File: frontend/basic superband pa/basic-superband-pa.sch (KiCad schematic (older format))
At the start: 59 parts, among them CN1 EDGE, CN2 BREAKOUT, K1 D3002, K2 D3002, P1 BNC, P2 CONN_02X01, P3 CONN_01X02, Q1 NPN, Q2 PNP, Q3 RD16HHF1, T1 TRANSFO, T2 8:1, T3 4:1, T4 OUT_TRANSF, U1 LP2951-50D

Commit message: Board files updated
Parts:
- added Q4: NPN, Transistors_SMD:sot23, symbol NPN
- added R10, R12: DNI, HERMESLITE:R_0805, symbol R
- added R11: 0, HERMESLITE:R_0805, symbol R
- added R9: 4.99k, HERMESLITE:R_0805, symbol R
- C22: value 47uF 16V -> 10uF 16V; footprint Discret:C1V8 -> Capacitors_Tantalum_SMD:TantalC_SizeB_EIA-3528_Reflow
- Q3: footprint Transistors_TO-220:TO-220_Neutral123_Horizontal -> Transistors_TO-220:TO-220_Neutral123_Vertical
- R8: value 2.21k -> 10k
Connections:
- wire segments 169 -> 181
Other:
- note added: "(Assuming CMOS inputs so\nbuffering to reduce loading.\nPTT# - RX=high, TX=low\nGPIO0 = BS0=low, BS1=high)"
- note added: "BAND 1"
- note added: "Band 0"
- note removed: "(RX=high, TX=low)"

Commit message: Upload latest pcb changes
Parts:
- removed CN2: BREAKOUT, Pin_Headers:Pin_Header_Straight_1x12, symbol BREAKOUT
- removed P3: CONN_01X02, Pin_Headers:Pin_Header_Straight_1x02, symbol CONN_01X02
- removed Q4: NPN, Transistors_SMD:sot23, symbol NPN
- removed R9: 4.99k, HERMESLITE:R_0805, symbol R
- added C25, C26, C27, C28: 0.01uF, HERMESLITE:C_0805, symbol C
- added C29: 0.1uF, HERMESLITE:C_0805, symbol C
- L10: footprint Choke_Axial_ThroughHole:Choke_Horizontal_RM10mm -> Choke_Toroid_ThroughHole:Choke_Toroid_horizontal_Diameter3-5mm_Amidon-T12
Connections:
- wire segments 181 -> 155
- no-connect marks 4 -> 17
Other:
- note added: "PTT# - RX=high, TX=low\nGPIO0 = BS0=low, BS1=high"
- note removed: "(Assuming CMOS inputs so\nbuffering to reduce loading.\nPTT# - RX=high, TX=low\nGPIO0 = BS0=low, BS1=high)"
- note removed: "Note: For superband PAs\nAlex protocol is disabled and \nGPIO0 is band select.\n\nCN2 will be removed after circuit prototype phase complete.\n\n"
- moved on the sheet: R1

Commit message: BOM updates
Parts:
- renumbered C8 to C11, C9 to C13, C11 to C14, C13 to C4, C4 to C5, C14 to C7, C5 to C8, C7 to C9, L3 to L2, L4 to L3, L2 to L4, L8 to L5, L5 to L7, L7 to L8
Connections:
- net at C11.1, K1.4 (T1), L7.1: now also C14.1
- net at K1.7 (T2), L5.2: no longer C14.1
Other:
- moved on the sheet: C14
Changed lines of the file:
@@
 GPIO0
 $Comp
-L INDUCTOR L5
+L INDUCTOR L7
 U 1 1 547D41C7
 P 3700 7450
-F 0 "L5" V 3650 7450 40  0000 C CNN
+F 0 "L7" V 3650 7450 40  0000 C CNN
 F 1 "INDUCTOR" V 3800 7450 40  0001 C CNN
 F 2 "Choke_Toroid_ThroughHole:Choke_Toroid_6,5x13mm_Vertical" H 3700 7450 60  0001 C CNN
@@
 $EndComp
 $Comp
-L C C8
+L C C11
 U 1 1 547D43ED
 P 3900 7150
-F 0 "C8" V 3850 6950 40  0000 L CNN
+F 0 "C11" V 3850 6950 40  0000 L CNN
 F 1 "C" H 3906 7065 40  0001 L CNN
 F 2 "HERMESLITE:C_0805" H 3938 7000 30  0001 C CNN
@@
 $EndComp
 $Comp
-L C C9
+L C C13
 U 1 1 547D44ED
 P 4700 7350
-F 0 "C9" H 4700 7450 40  0000 L CNN
+F 0 "C13" H 4700 7450 40  0000 L CNN
 F 1 "C" H 4706 7265 40  0001 L CNN
 F 2 "HERMESLITE:C_0805" H 4738 7200 30  0001 C CNN
@@
 $EndComp
 $Comp
-L INDUCTOR L7
+L INDUCTOR L8
 U 1 1 547D4686
 P 4850 7450
-F 0 "L7" V 4800 7450 40  0000 C CNN
+F 0 "L8" V 4800 7450 40  0000 C CNN
 F 1 "INDUCTOR" V 4950 7450 40  0001 C CNN
 F 2 "Choke_Toroid_ThroughHole:Choke_Toroid_6,5x13mm_Vertical" H 4850 7450 60  0001 C CNN
@@
 $EndComp
 $Comp
-L INDUCTOR L8
+L INDUCTOR L5
 U 1 1 547D490A
 P 5550 7150
-F 0 "L8" V 5500 7150 40  0000 C CNN
+F 0 "L5" V 5500 7150 40  0000 C CNN
 F 1 "INDUCTOR" V 5650 7150 40  0001 C CNN
 F 2 "Choke_Toroid_ThroughHole:Choke_Toroid_6,5x13mm_Vertical" H 5550 7150 60  0001 C CNN
@@
 $EndComp
 $Comp
-L C C11
+L C C14
 U 1 1 547D4975
-P 5850 7350
-F 0 "C11" H 5850 7450 40  0000 L CNN
-F 1 "C" H 5856 7265 40  0001 L CNN
-F 2 "HERMESLITE:C_0805" H 5888 7200 30  0001 C CNN
-F 3 "" H 5850 7350 60  0000 C CNN
-	1    5850 7350
-	1    0    0    -1
-$EndComp
-$Comp
-L INDUCTOR L4
+P 3450 7350
+F 0 "C14" H 3450 7450 40  0000 L CNN
+F 1 "C" H 3456 7265 40  0001 L CNN
+F 2 "HERMESLITE:C_0805" H 3488 7200 30  0001 C CNN
+F 3 "" H 3450 7350 60  0000 C CNN
+	1    3450 7350
+	1    0    0    -1
+$EndComp
+$Comp
+L INDUCTOR L3
 U 1 1 547D4CF1
 P 6000 6500
-F 0 "L4" V 5950 6500 40  0000 C CNN
+F 0 "L3" V 5950 6500 40  0000 C CNN
 F 1 "INDUCTOR" V 6100 6500 40  0001 C CNN
 F 2 "Choke_Toroid_ThroughHole:Choke_Toroid_6,5x13mm_Vertical" H 6000 6500 60  0001 C CNN
@@
 $EndComp
 $Comp
-L C C4
+L C C5
 U 1 1 547D4CF8
 P 4500 6200
-F 0 "C4" V 4450 6300 40  0000 L CNN
+F 0 "C5" V 4450 6300 40  0000 L CNN
 F 1 "C" H 4506 6115 40  0001 L CNN
 F 2 "HERMESLITE:C_0805" H 4538 6050 30  0001 C CNN
@@
 $EndComp
 $Comp
-L C C5
+L C C8
 U 1 1 547D4D04
 P 4700 6400
-F 0 "C5" H 4700 6500 40  0000 L CNN
+F 0 "C8" H 4700 6500 40  0000 L CNN
 F 1 "C" H 4706 6315 40  0001 L CNN
 F 2 "HERMESLITE:C_0805" H 4738 6250 30  0001 C CNN
@@
 $EndComp
 $Comp
-L INDUCTOR L2
+L INDUCTOR L4
 U 1 1 547D4D0B
 P 4850 6500
-F 0 "L2" V 4800 6500 40  0000 C CNN
+F 0 "L4" V 4800 6500 40  0000 C CNN
 F 1 "INDUCTOR" V 4950 6500 40  0001 C CNN
 F 2 "Choke_Toroid_ThroughHole:Choke_Toroid_6,5x13mm_Vertical" H 4850 6500 60  0001 C CNN
@@
 $EndComp
 $Comp
-L INDUCTOR L3
+L INDUCTOR L2
 U 1 1 547D4D17
 P 5150 6200
-F 0 "L3" V 5100 6200 40  0000 C CNN
+F 0 "L2" V 5100 6200 40  0000 C CNN
 F 1 "INDUCTOR" V 5250 6200 40  0001 C CNN
 F 2 "Choke_Toroid_ThroughHole:Choke_Toroid_6,5x13mm_Vertical" H 5150 6200 60  0001 C CNN
@@
 $EndComp
 $Comp
-L C C7
+L C C9
 U 1 1 547D4D1D
 P 5850 6400
-F 0 "C7" H 5850 6500 40  0000 L CNN
+F 0 "C9" H 5850 6500 40  0000 L CNN
 F 1 "C" H 5856 6315 40  0001 L CNN
 F 2 "HERMESLITE:C_0805" H 5888 6250 30  0001 C CNN
@@
 L GND #PWR012
 U 1 1 547D5D63
-P 5850 7550
-F 0 "#PWR012" H 5850 7550 30  0001 C CNN
-F 1 "GND" H 5850 7480 30  0001 C CNN
-F 2 "" H 5850 7550 60  0000 C CNN
-F 3 "" H 5850 7550 60  0000 C CNN
-	1    5850 7550
+P 3450 7550
+F 0 "#PWR012" H 3450 7550 30  0001 C CNN
+F 1 "GND" H 3450 7480 30  0001 C CNN
+F 2 "" H 3450 7550 60  0000 C CNN
+F 3 "" H 3450 7550 60  0000 C CNN
+	1    3450 7550
 	1    0    0    -1
 $EndComp
@@
 $EndComp
 $Comp
-L CP1 C14
+L CP1 C7
 U 1 1 54872CD7
 P 5250 1750
-F 0 "C14" H 5300 1850 50  0000 L CNN
+F 0 "C7" H 5300 1850 50  0000 L CNN
 F 1 "47uF 16V" H 5400 1750 50  0000 L CNN
 F 2 "Discret:C1V8" H 5250 1750 60  0001 C CNN
@@
 $EndComp
 $Comp
-L C C13
+L C C4
 U 1 1 54872F5F
 P 5000 1750
-F 0 "C13" H 5000 1850 40  0000 L CNN
+F 0 "C4" H 5000 1850 40  0000 L CNN
 F 1 "0.1uF" H 4800 1850 40  0000 L CNN
 F 2 "HERMESLITE:C_0805" H 5038 1600 30  0001 C CNN
@@
 	1    0    0    -1
 $EndComp
-Text Notes 2550 7600 0    40   ~ 0
+Text Notes 2450 7550 0    40   ~ 0
 (Omit K2 and wire directly \nif only 1 band pair desired)
 $Comp
@@
 Connection ~ 4850 7750
 Connection ~ 4700 7550
-Connection ~ 5850 7550
+Connection ~ 3450 7550
 Connection ~ 3700 7750
 Connection ~ 4700 6600
@@
 Wire Wire Line
 	10200 5400 10200 6000
+Connection ~ 3450 7150
 $EndSCHEMATC

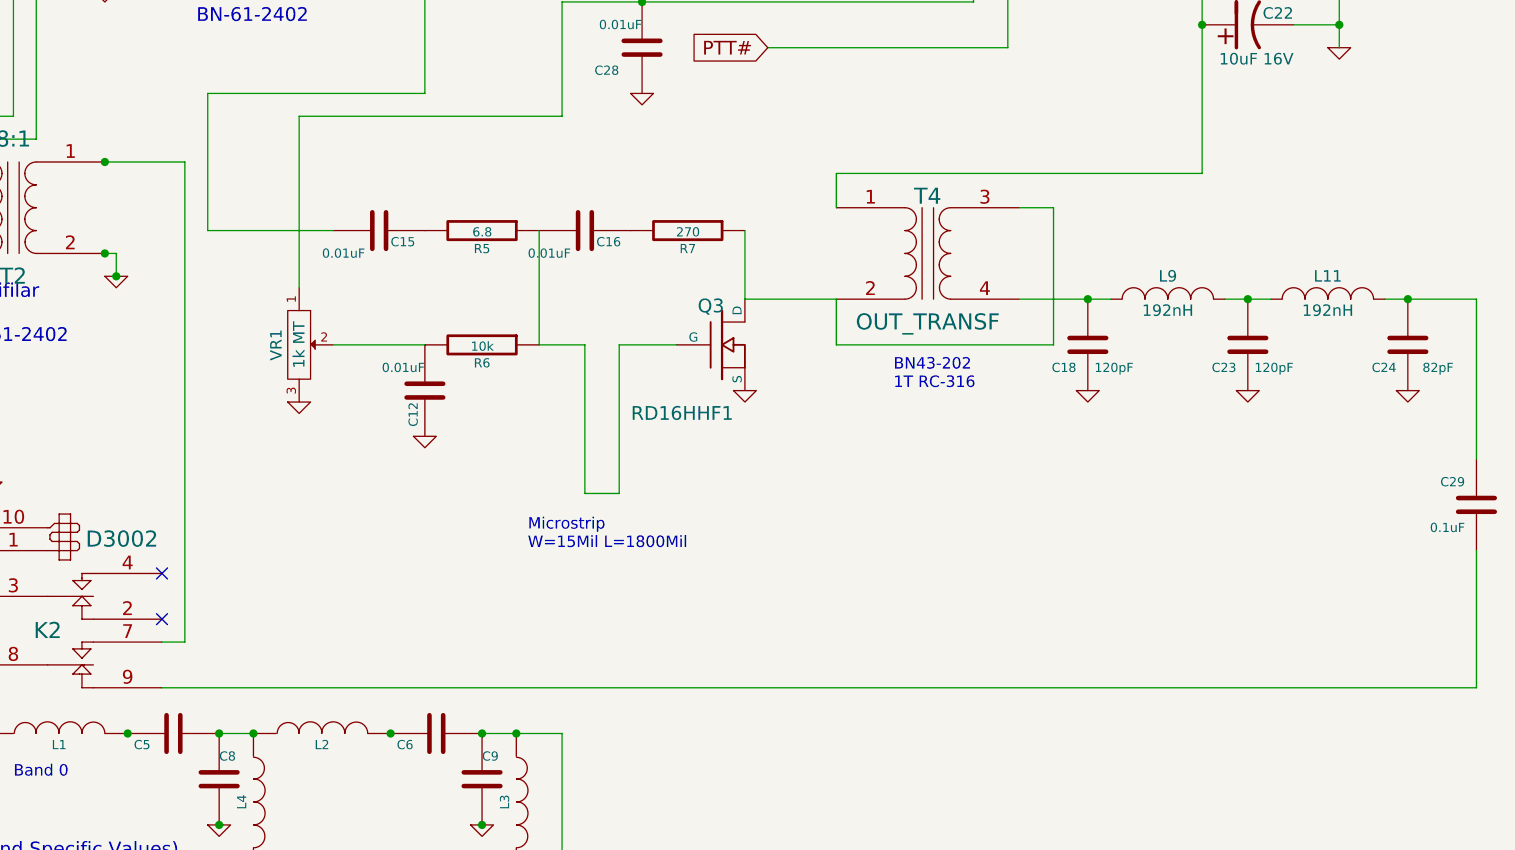
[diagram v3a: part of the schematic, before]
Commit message: Correct compnent naming and fix relay error
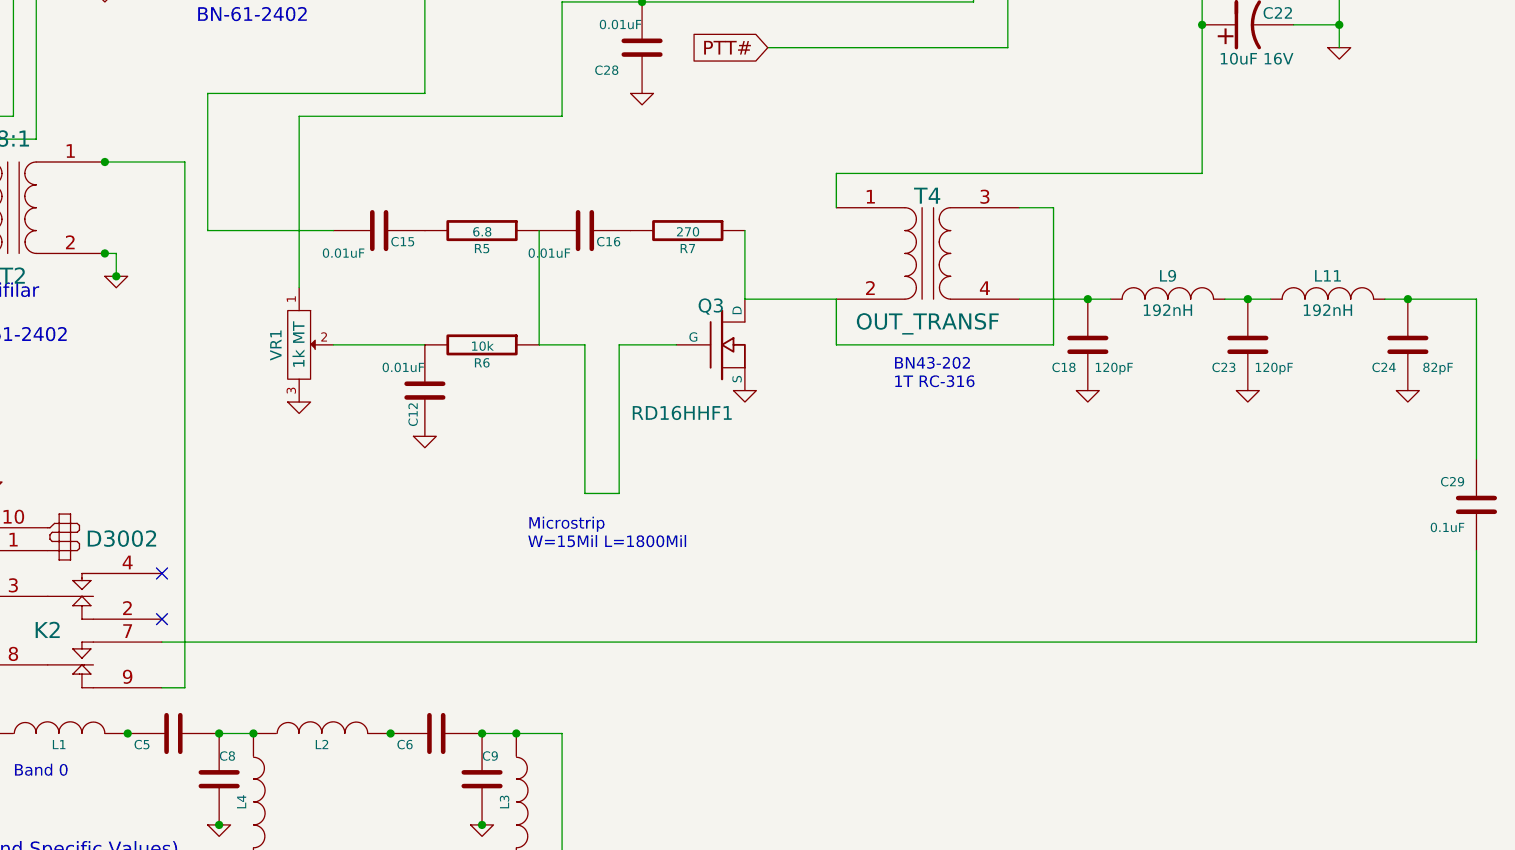
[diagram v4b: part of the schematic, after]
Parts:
- C22: footprint Capacitors_Tantalum_SMD:TantalC_SizeB_EIA-3528_Reflow -> Capacitors_SMD:C_1206
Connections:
- net at T2.1 (S1): now also K2.9 (R2); no longer K2.7 (T2)
- net at C29.1: now also K2.7 (T2); no longer K2.9 (R2)
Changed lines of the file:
@@
 F 0 "C22" V 9250 2900 50  0000 L CNN
 F 1 "10uF 16V" V 9050 2900 50  0000 L CNN
-F 2 "Capacitors_Tantalum_SMD:TantalC_SizeB_EIA-3528_Reflow" H 9200 3100 60  0001 C CNN
+F 2 "Capacitors_SMD:C_1206" H 9200 3100 60  0001 C CNN
 F 3 "" H 9200 3100 60  0000 C CNN
 	1    9200 3100
@@
 	1    2700 5650
 	1    0    0    -1
-$EndComp
-$Comp
-L D3002 K2
-U 1 1 54AF7B3F
-P 4050 5650
-F 0 "K2" H 3950 5750 70  0000 C CNN
-F 1 "D3002" H 4275 5350 70  0000 C CNN
-F 2 "HERMESLITE:D3002" H 4050 5650 60  0001 C CNN
-F 3 "" H 4050 5650 60  0000 C CNN
-	1    4050 5650
-	1    0    0    1
 $EndComp
 $Comp
@@
 	2400 7050 2500 7050
 Wire Wire Line
-	4550 3700 4550 5800
+	4550 3700 4550 6000
 Wire Wire Line
 	3400 4650 3400 4600
@@
 	3200 5900 3650 5900
 Wire Wire Line
-	4550 5800 4450 5800
-Wire Wire Line
 	3700 5100 3700 5000
 Wire Wire Line
@@
 Wire Wire Line
 	3600 5300 3650 5300
-Wire Wire Line
-	10200 6000 4450 6000
 Wire Wire Line
 	6450 5150 6300 5150
@@
 Wire Wire Line
 	10200 4300 10200 5000
-Wire Wire Line
-	10200 5400 10200 6000
 Connection ~ 3450 7150
+$Comp
+L D3002 K2
+U 1 1 54AF7B3F
+P 4050 5650
+F 0 "K2" H 3950 5750 70  0000 C CNN
+F 1 "D3002" H 4275 5350 70  0000 C CNN
+F 2 "HERMESLITE:D3002" H 4050 5650 60  0001 C CNN
+F 3 "" H 4050 5650 60  0000 C CNN
+	1    4050 5650
+	1    0    0    1
+$EndComp
+Wire Wire Line
+	4550 6000 4450 6000
+Wire Wire Line
+	4450 5800 10200 5800
+Wire Wire Line
+	10200 5800 10200 5400
 $EndSCHEMATC

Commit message: Few more pcb changes
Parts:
- added JP1: JUMPER4, HERMESLITE:JUMPER4, symbol JUMPER4
- added R13: 4.99k, HERMESLITE:R_0805, symbol R
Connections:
- net GND: now also JP1.1
- net GPIO0: now also JP1.4; no longer R1.2
- net at C17.1, C26.2, C4.1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: now also R13.1
- new net: JP1.2, R1.2
- new net: JP1.3, R13.2
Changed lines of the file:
@@
 	1    0    0    -1
 $EndComp
-Text GLabel 1800 5650 0    60   Input ~ 0
+Text GLabel 1150 5650 0    60   Input ~ 0
 GPIO0
 Text GLabel 3900 1350 2    60   Output ~ 0
@@
 Text Notes 1400 7350 0    50   ~ 0
 BN-61-2402\n  2x4T #30
-Text Notes 1050 5350 0    60   ~ 0
+Text Notes 1500 4550 0    60   ~ 0
 PTT# - RX=high, TX=low\nGPIO0 = BS0=low, BS1=high
 Text Notes 3600 6750 0    60   ~ 0
@@
 Connection ~ 6550 3000
 Wire Wire Line
-	1800 5650 1900 5650
-Wire Wire Line
 	2400 5650 2500 5650
 Wire Wire Line
@@
 Connection ~ 2400 5650
 Connection ~ 2500 5650
-Connection ~ 1900 5650
 $Comp
 L C C26
@@
 Wire Wire Line
 	10200 5800 10200 5400
+$Comp
+L JUMPER4 JP1
+U 1 1 54BD04F7
+P 1650 5650
+F 0 "JP1" V 1750 5750 40  0000 L CNN
+F 1 "JUMPER4" V 1500 5450 40  0000 C CNN
+F 2 "HERMESLITE:JUMPER4" H 1650 5650 60  0001 C CNN
+F 3 "" H 1650 5650 60  0000 C CNN
+	1    1650 5650
+	0    -1   -1   0
+$EndComp
+$Comp
+L GND #PWR035
+U 1 1 54BD0629
+P 1650 5900
+F 0 "#PWR035" H 1650 5900 30  0001 C CNN
+F 1 "GND" H 1650 5830 30  0001 C CNN
+F 2 "" H 1650 5900 60  0000 C CNN
+F 3 "" H 1650 5900 60  0000 C CNN
+	1    1650 5900
+	1    0    0    -1
+$EndComp
+Wire Wire Line
+	1750 5650 1900 5650
+Wire Wire Line
+	1150 5650 1400 5650
+$Comp
+L R R13
+U 1 1 54BD0931
+P 1900 5400
+F 0 "R13" V 1980 5400 40  0000 C CNN
+F 1 "4.99k" V 1907 5401 40  0000 C CNN
+F 2 "HERMESLITE:R_0805" V 1830 5400 30  0001 C CNN
+F 3 "" H 1900 5400 30  0000 C CNN
+	1    1900 5400
+	0    1    1    0
+$EndComp
+Wire Wire Line
+	1300 5250 2200 5250
+Wire Wire Line
+	2200 5250 2200 5400
+Wire Wire Line
+	2200 5400 2150 5400
+Connection ~ 1300 5250
 $EndSCHEMATC

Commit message: Final pcd changes
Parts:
- added Q2-next: FDV301, symbol MOS_N
- R8: value 10k -> DNI
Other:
- note added: "DNI?"
- note added: "Need to pull up gate\nwith 10K to 3.3V"
- note added: "Remove in\nnext revision"
- note added: "Remove on next revision"
- note added: "Replace with 0R0"
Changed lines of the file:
@@
 	1    0    0    -1
 $EndComp
-Text Notes 3550 4500 0    60   ~ 0
+Text Notes 4000 3600 0    60   ~ 0
 6T bifilar\n4T\nBN-61-2402
 Text Notes 4600 3100 0    60   ~ 0
@@
 Text Notes 1400 7350 0    50   ~ 0
 BN-61-2402\n  2x4T #30
-Text Notes 1500 4550 0    60   ~ 0
+Text Notes 1700 4400 0    60   ~ 0
 PTT# - RX=high, TX=low\nGPIO0 = BS0=low, BS1=high
 Text Notes 3600 6750 0    60   ~ 0
@@
 P 8150 1800
 F 0 "R8" V 8230 1800 40  0000 C CNN
-F 1 "10k" V 8157 1801 40  0000 C CNN
+F 1 "DNI" V 8157 1801 40  0000 C CNN
 F 2 "HERMESLITE:R_0805" V 8080 1800 30  0001 C CNN
 F 3 "" H 8150 1800 30  0000 C CNN
@@
 	2200 5400 2150 5400
 Connection ~ 1300 5250
+Text Notes 7800 2100 0    50   ~ 10
+Remove on next revision
+$Comp
+L MOS_N Q2-next
+U 1 1 54C3289A
+P 4050 4850
+F 0 "Q2-next" H 4150 5100 60  0000 R CNN
+F 1 "FDV301" H 3950 4750 60  0000 R CNN
+F 2 "" H 4050 4850 60  0000 C CNN
+F 3 "" H 4050 4850 60  0000 C CNN
+	1    4050 4850
+	1    0    0    -1
+$EndComp
+Wire Notes Line
+	3500 4850 3800 4850
+Wire Notes Line
+	3450 4650 4050 4650
+Wire Notes Line
+	4100 5050 3750 5050
+Wire Notes Line
+	3450 5050 3550 5050
+Text Notes 2100 4750 0    50   ~ 10
+Replace with 0R0
+Text Notes 2350 5100 0    50   ~ 10
+DNI?
+Text Notes 2900 4650 0    50   ~ 10
+Need to pull up gate\nwith 10K to 3.3V
+Wire Notes Line
+	1450 5150 1450 6000
+Wire Notes Line
+	1450 6000 1950 6000
+Wire Notes Line
+	1950 6000 1950 5150
+Wire Notes Line
+	1950 5150 1450 5150
+Text Notes 1450 5100 0    50   ~ 10
+Remove in\nnext revision
 $EndSCHEMATC
